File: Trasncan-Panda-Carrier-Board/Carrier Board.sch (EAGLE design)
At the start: 56 parts, among them J1 B2B-PH-SM4-TB(LF)(SN), J2 B2B-PH-SM4-TB(LF)(SN), J3 BM04B-SRSS-TBT(LF)(SN), J4 BM06B-SRSS-TBT(LF)(SN), J5 BM06B-SRSS-TBT(LF)(SN), J6 BM06B-SRSS-TBT(LF)(SN), J7 BM04B-SRSS-TBT(LF)(SN), J8 BM04B-SRSS-TBT(LF)(SN), J9 BM04B-SRSS-TBT(LF)(SN), P1 Particle Boron / Xenon / Argon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

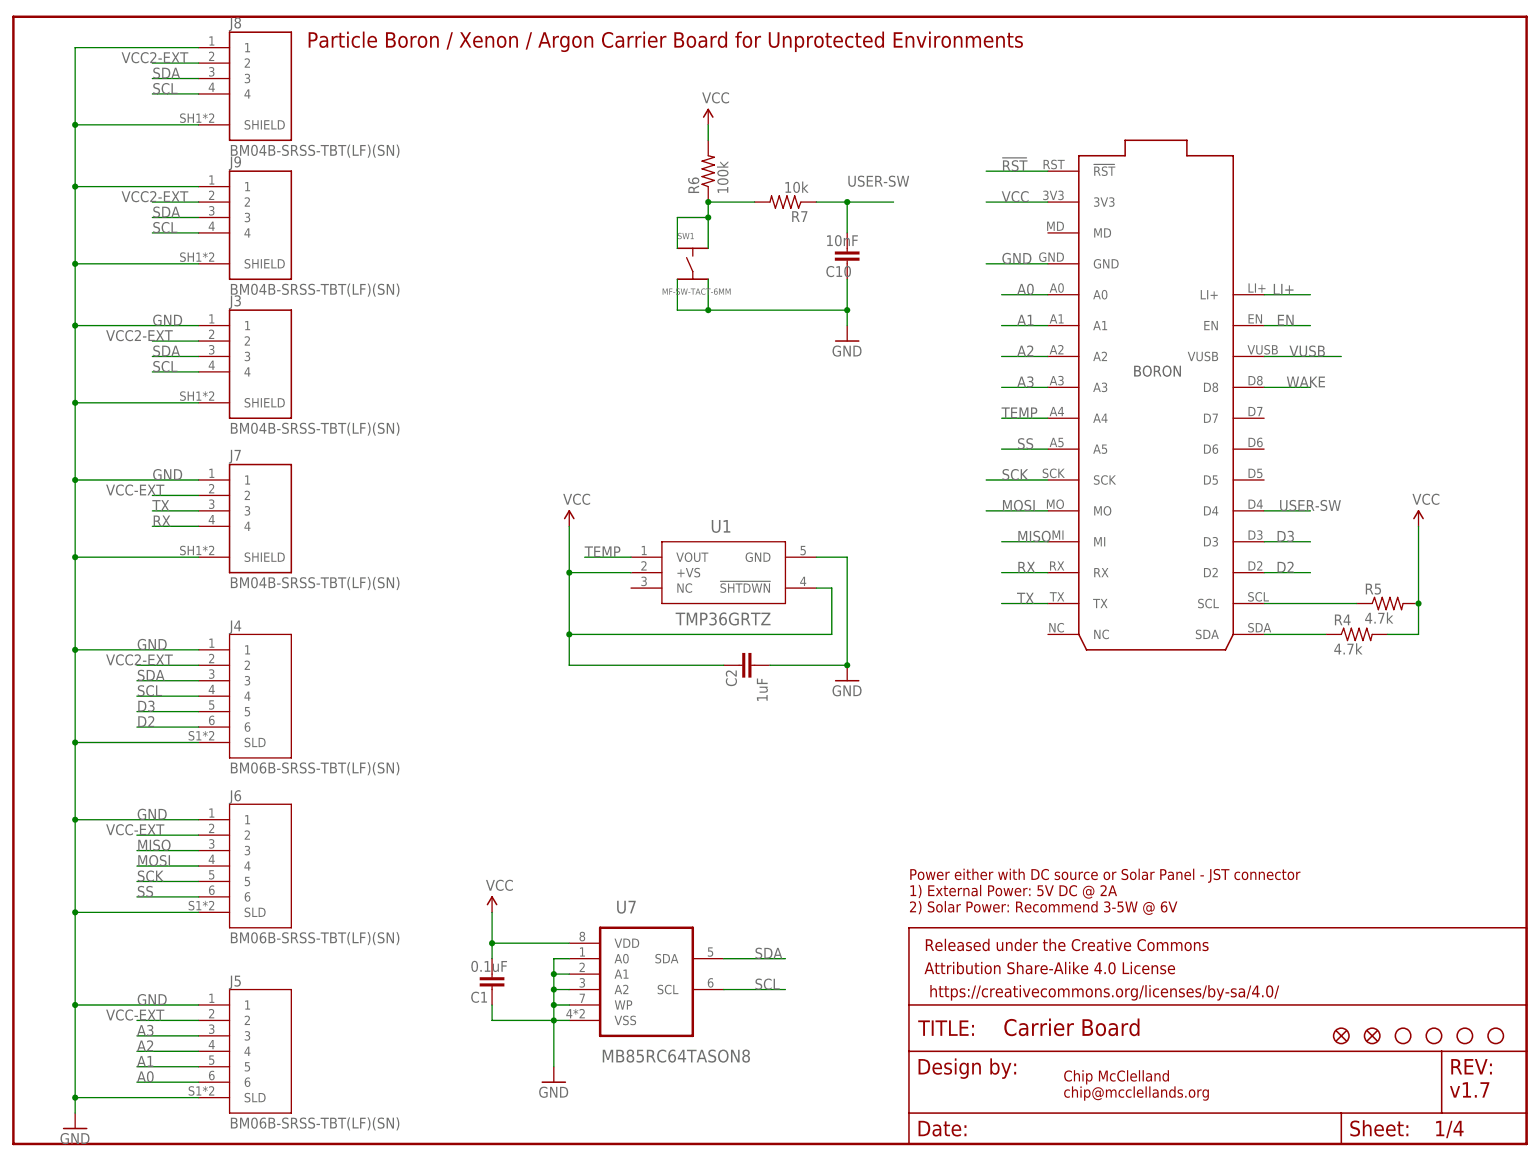
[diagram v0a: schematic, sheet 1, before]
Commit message: Rectangular Sensor Board
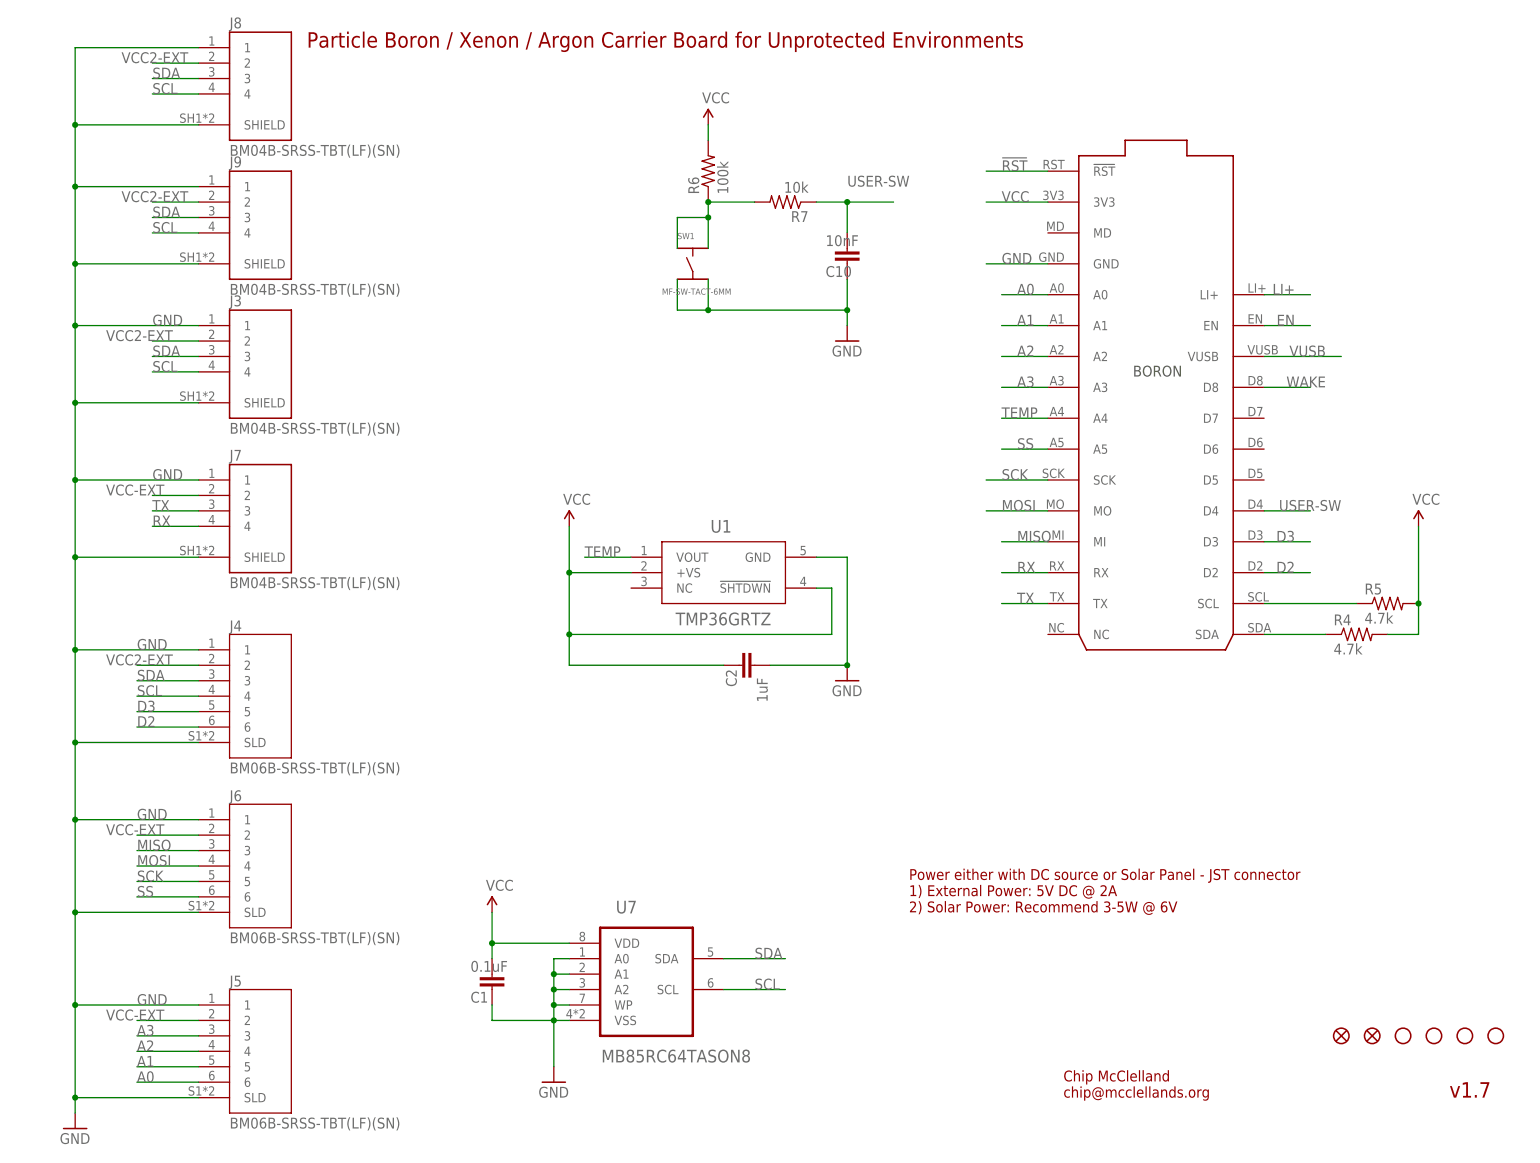
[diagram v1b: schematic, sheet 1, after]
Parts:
- removed FRAME1, FRAME2, FRAME3: FRAME-LETTER, SparkFun-Aesthetics:FRAME-LETTER
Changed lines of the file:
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@@
 <attribute name="MPN" value="0466.500NR"/>
-</part>
-<part name="FRAME1" library="SparkFun-Aesthetics" library_urn="urn:adsk.eagle:library:507" deviceset="FRAME-LETTER" device="" package3d_urn="urn:adsk.eagle:package:37121/1">
-<attribute name="POPULATE" value="0"/>
-</part>
-<part name="FRAME2" library="SparkFun-Aesthetics" library_urn="urn:adsk.eagle:library:507" deviceset="FRAME-LETTER" device="" package3d_urn="urn:adsk.eagle:package:37121/1">
-<attribute name="POPULATE" value="0"/>
 </part>
 <part name="R7" library="Custom Components" deviceset="RESISTOR-MF-10K-" device="0805" package3d_urn="urn:adsk.eagle:package:39651/1" value="10k">
@@
 <attribute name="HOUSEPART" value="Yes"/>
 <attribute name="MPN" value="MF-CAP-0805-0.1uF"/>
-</part>
-<part name="FRAME3" library="SparkFun-Aesthetics" library_urn="urn:adsk.eagle:library:507" deviceset="FRAME-LETTER" device="" package3d_urn="urn:adsk.eagle:package:37121/1">
-<attribute name="POPULATE" value="0"/>
 </part>
 <part name="JP7" library="SparkFun-Jumpers" library_urn="urn:adsk.eagle:library:528" deviceset="JUMPER-SMT_2_NO" device="_SILK" package3d_urn="urn:adsk.eagle:package:39279/1">
@@
 <instance part="GND5" gate="1" x="137.16" y="132.08" smashed="yes">
 <attribute name="VALUE" x="134.62" y="129.54" size="1.778" layer="96"/>
-</instance>
-<instance part="FRAME1" gate="G$1" x="0" y="0" smashed="yes">
-<attribute name="POPULATE" x="0" y="0" size="1.778" layer="96" display="off"/>
-</instance>
-<instance part="FRAME1" gate="V" x="147.32" y="0" smashed="yes">
-<attribute name="LAST_DATE_TIME" x="160.02" y="1.27" size="2.54" layer="94" font="vector"/>
-<attribute name="SHEET" x="233.68" y="1.27" size="2.54" layer="94" font="vector"/>
-<attribute name="DRAWING_NAME" x="162.814" y="17.78" size="2.7432" layer="94" font="vector"/>
 </instance>
 <instance part="R7" gate="G$1" x="127" y="154.94" smashed="yes" rot="R180">
@@
 </plain>
 <instances>
-<instance part="FRAME2" gate="G$1" x="0" y="0" smashed="yes">
-<attribute name="POPULATE" x="0" y="0" size="1.778" layer="96" display="off"/>
-</instance>
-<instance part="FRAME2" gate="V" x="147.32" y="0" smashed="yes">
-<attribute name="LAST_DATE_TIME" x="160.02" y="1.27" size="2.54" layer="94" font="vector"/>
-<attribute name="SHEET" x="233.68" y="1.27" size="2.54" layer="94" font="vector"/>
-<attribute name="DRAWING_NAME" x="162.814" y="17.78" size="2.7432" layer="94" font="vector"/>
-</instance>
 <instance part="GND10" gate="1" x="116.84" y="50.8" smashed="yes">
 <attribute name="VALUE" x="116.84" y="50.546" size="1.778" layer="96" align="top-center"/>
@@
 </plain>
 <instances>
-<instance part="FRAME3" gate="G$1" x="0" y="0" smashed="yes">
-<attribute name="POPULATE" x="0" y="0" size="1.778" layer="96" display="off"/>
-</instance>
-<instance part="FRAME3" gate="V" x="147.32" y="0" smashed="yes">
-<attribute name="LAST_DATE_TIME" x="160.02" y="1.27" size="2.54" layer="94" font="vector"/>
-<attribute name="SHEET" x="233.68" y="1.27" size="2.54" layer="94" font="vector"/>
-<attribute name="DRAWING_NAME" x="162.814" y="17.78" size="2.7432" layer="94" font="vector"/>
-</instance>
 <instance part="U3" gate="A" x="162.56" y="96.52" smashed="yes">
 <attribute name="NAME" x="157.8356" y="113.2586" size="2.0828" layer="95" ratio="6" rot="SR0"/>
